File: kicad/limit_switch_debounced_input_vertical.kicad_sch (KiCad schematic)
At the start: 4 parts, among them J1601 TBH-1x02-3.5mm, U1601 MAX6816

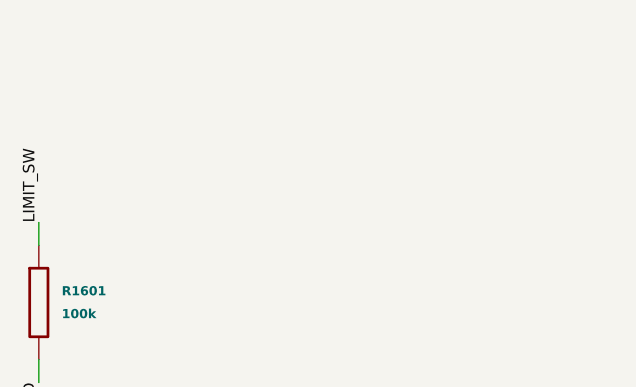
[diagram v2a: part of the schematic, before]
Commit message: Update limit switch block
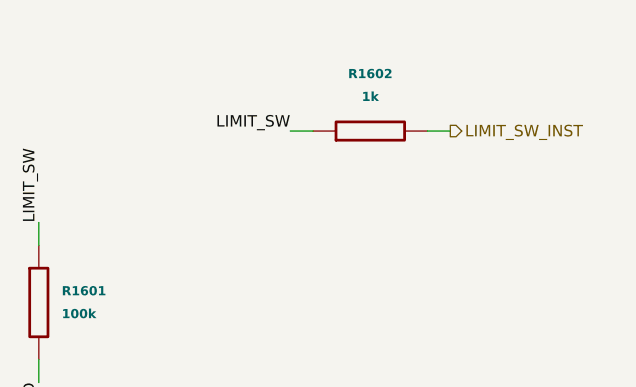
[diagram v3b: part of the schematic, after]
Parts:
- added R1602: 1k, Resistor_SMD:R_0402_1005Metric, symbol orb_weaver_internal:All/OW-PASS-RC0402FR-071KL
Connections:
- net LIMIT_SW: now also R1602.1
- new net LIMIT_SW_INST: R1602.2
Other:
- company: Janelia Research Campus -> (none)
- title: mouse-joystick-pcb -> Orb Weaver Design Block Mining

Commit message: Regenerate schematics
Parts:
- C1601: JLC Qty 9978 -> (none); LCSC C162178 -> (none); Placement (none) -> beside ${ed1d27a5-4fdc-4e73-a297-77a8487eb0d8:REFERENCE}.4 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; Vendor SKU C162178 -> (none)
- J1601: JLC Qty 148 -> (none); LCSC C3019639 -> (none); Vendor SKU C3019639 -> (none)
- R1601: JLC Qty 9963 -> (none); LCSC C106234 -> (none); Placement (none) -> beside ${ed1d27a5-4fdc-4e73-a297-77a8487eb0d8:REFERENCE}.3 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; Vendor SKU C106234 -> (none)
- R1602: JLC Qty 10129 -> (none); LCSC C106235 -> (none); Vendor SKU C106235 -> (none)
- U1601: value MAX6816 -> MAX6816EUS+T; JLC Qty 98 -> (none); LCSC C41637 -> (none); Name MAX6816 -> MAX6816 switch debouncer; ReqValue MAX6816 -> MAX6816EUS+T; Vendor SKU C41637 -> (none)
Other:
- note added: "${1a5dbbac-981b-4337-8c39-817e15b42b3f:REFERENCE} (100 k) holds LIMIT_SW low while the debouncer is unpowered; ${fb894a4c-a934-4f36-81fc-dbadc5d06e8e:REFERENCE} (1 k) is the series tap from LIMIT_SW to LIMIT_SW_INST."
- note added: "${1a5dbbac-981b-4337-8c39-817e15b42b3f:REFERENCE}, 100 kohm from LIMIT_SW to GND (OW-PASS-RC0402JR-07100KL, LCSC C106234), is what defines it while that domain is down, and it is"
- note added: "${1a5dbbac-981b-4337-8c39-817e15b42b3f:REFERENCE}: Output pull-down for the unpowered state"
- note added: "${877edc0d-8517-4bfb-9a8a-87ef2f65742a:REFERENCE}: Vcc bypass for ${ed1d27a5-4fdc-4e73-a297-77a8487eb0d8:REFERENCE}"
- note added: "${fb560492-07c1-40ba-abbe-6bac76e602ff:REFERENCE} brings the dry contact onto IN (pin 2) and GND (pin 1); ${ed1d27a5-4fdc-4e73-a297-77a8487eb0d8:REFERENCE} debounces IN and drives LIMIT_SW from its push-pull OUT. ${877edc0d-8517-4bfb-9a8a-87ef2f65742a:REFERENCE} (100 nF) bypasses Vcc (pin 4) to GND (pin 1)."
- note added: "+3.3V_SW is off."
- note added: "0.200 mm netclass rule. Move a run before widening it and re-run DRC after any change here."
- note added: "0.4 mm on these centres is a 0.100 mm gap, which sits exactly on the JLCPCB routine copper floor in .kicad_dru and errors under any 0.2 mm"
- note added: "1. Switch terminal and debouncer"
- note added: "100 kohm AND NOT 10 kohm: this net idles HIGH, since a normally-open contact plus the internal IN pull-up puts OUT high whenever the axis is away"
- note added: "2. Output pull-down and instrument tap"
- note added: "Bring REFL to a labelled test pad at board level so a jumper can force a closure during bring-up. Add no capacitor on IN — it fights the debounce"
- note added: "Connect a dry-contact mechanical switch across the terminal; pin 1 is GND, pin 2 is the switch node, and the contact is polarity-agnostic. OUT"
- note added: "DESIGN CONTRACT"
- note added: "Debounced limit-switch input with its own 2-position 3.5 mm VERTICAL, top-entry pluggable screw terminal — Phoenix MCV 1,5/2-G-3,5,"
- note added: "Debounced limit-switch input with its own 2-position 3.5 mm VERTICAL, top-entry pluggable screw terminal — Phoenix MCV 1,5/2-G-3,5, OW-CONN-TBH-1X02-3P5-VERT, on the local orb_weaver_tht copy of the MCV footprint — plus a MAX6816 single switch debouncer and local Vcc decoupling."
- note added: "Debounced limit-switch input, vertical terminal | MAX6816, output pull-down, instrument tap"
- note added: "Debounced switch state, active low on contact closure and about 50 ms late; push-pull at Vcc levels while powered, held low by ${1a5dbbac-981b-4337-8c39-817e15b42b3f:REFERENCE} when"
- note added: "Debouncer supply, 2.7 to 5.5 V; bind it to the switched domain of whatever LIMIT_SW drives, so the debouncer cannot back-power a powered-down"
- note added: "Electrically identical to the horizontal limit_switch_debounced_input block, port for port and part for part including the pull-down: +3.3V_SW, GND,"
- note added: "GND, pin 2 IN"
- note added: "GND. A closed contact pulls IN low; OUT follows IN non-inverting after the debounce (20 to 80 ms, 50 ms typical), so LIMIT_SW is active low and"
- note added: "IN is complete inside ${ed1d27a5-4fdc-4e73-a297-77a8487eb0d8:REFERENCE}: internal pull-up 63 k typical, -25 to +25 V range, +/-15 kV air-gap ESD. No external pull-up, series resistor or"
- note added: "INTERFACES"
- note added: "IS THEREFORE 0.3 mm, not the 0.4 mm it was authored at, which puts the LIMIT_SW-to-GND gap at exactly 0.200 mm against a 0.200 mm netclass"
- note added: "Instrument tap of LIMIT_SW through ${fb894a4c-a934-4f36-81fc-dbadc5d06e8e:REFERENCE} (1 k), INSTRUMENT class; reads asserted while the switched rail is off."
- note added: "Instrument tap series resistor"
- note added: "KNOW THE POLARITY CONSEQUENCE BEFORE TRUSTING A CAPTURE: LIMIT_SW is active low, so this resistor makes an instrument tap read ASSERTED, limit"
- note added: "LIMIT_SW."
- note added: "Matching net labels are connected. Group order explains function; PCB placement priorities are stated below."
- note added: "OPERATION"
- note added: "OW-CONN-TBH-1X02-3P5-VERT, on the local orb_weaver_tht copy of the MCV footprint — plus a MAX6816 single switch debouncer and local Vcc"
- note added: "PLACE: ${1a5dbbac-981b-4337-8c39-817e15b42b3f:REFERENCE} sits above ${ed1d27a5-4fdc-4e73-a297-77a8487eb0d8:REFERENCE} with its LIMIT_SW pad on the OUT side, so LIMIT_SW and GND never need to cross; ${fb894a4c-a934-4f36-81fc-dbadc5d06e8e:REFERENCE} goes where LIMIT_SW leaves toward the"
- note added: "PLACE: Keep ${ed1d27a5-4fdc-4e73-a297-77a8487eb0d8:REFERENCE} next to ${fb560492-07c1-40ba-abbe-6bac76e602ff:REFERENCE} so IN stays short; nothing else connects to IN. Leave the 4.75 mm inboard keepout of the vertical terminal free, and give the enclosure an aperture"
- note added: "PLACE: Place ${877edc0d-8517-4bfb-9a8a-87ef2f65742a:REFERENCE} hard against pin 4 with a short return to pin 1."
- note added: "Project-local pending bench verification; promotable once a second board uses it."
- note added: "REQUIRED, not optional: THE MAX6816 HAS NO Ioff. With Vcc at 0 V its push-pull OUT is undefined, and a board that taps LIMIT_SW for instrumentation"
- note added: "ROUTE: +3.3V_SW has no reference-project class here (Default); the placing board classes the switched rail."
- note added: "ROUTE: LIMIT_SW and LIMIT_SW_INST leave through vias (port copper); LIMIT_SW_INST carries the INSTRUMENT class."
- note added: "ROUTE: The LIMIT_SW and GND runs share the corridor bounded by the IN pad on 0.5 mm centres: every track in the block is 0.3 mm, which leaves the LIMIT_SW-to-GND gap at exactly the"
- note added: "ROUTING THE PULL-DOWN IS TIGHT, AND IT IS AT THE LIMIT: ${1a5dbbac-981b-4337-8c39-817e15b42b3f:REFERENCE} sits above the MAX6816 with its LIMIT_SW pad on the same side as the IC's OUT"
- note added: "Return; terminal pin 1 (the switch's other side), the Vcc bypass and the output pull-down."
- note added: "Same circuit as limit_switch_debounced_input plus the tap. ${fb560492-07c1-40ba-abbe-6bac76e602ff:REFERENCE} (Phoenix MCV 1,5/2-G-3,5) is pad-identical to the horizontal MC 1,5 but"
- note added: "Signal path: ${fb560492-07c1-40ba-abbe-6bac76e602ff:REFERENCE} pin 2 -> IN -> ${ed1d27a5-4fdc-4e73-a297-77a8487eb0d8:REFERENCE} IN (pin 2) -> OUT (pin 3) -> LIMIT_SW, tapped through ${fb894a4c-a934-4f36-81fc-dbadc5d06e8e:REFERENCE} to LIMIT_SW_INST; ${fb560492-07c1-40ba-abbe-6bac76e602ff:REFERENCE} pin 1 is"
- note added: "Supply +3.3V from the SWITCHED power domain on any board where LIMIT_SW drives a chip that can be powered down: if the debouncer stays alive"
- note added: "Supply 2.7 to 5.5 V at 6 uA typical (UVLO 1.9 to 2.6 V). ${1a5dbbac-981b-4337-8c39-817e15b42b3f:REFERENCE} (100 k) defines LIMIT_SW low while +3.3V_SW is off, since the MAX6816 has no Ioff;"
- note added: "Switch debouncer"
- note added: "THIS BLOCK IS A FORK BY CHOICE, NOT BY GEOMETRY. Unlike usb2_vertical and pycontrol_behavior_port_rj45_boundary_vertical, whose land patterns are"
- note added: "Vertical switch terminal, pin 1"
- note added: "What actually changes is the mechanical envelope, and it inverts. Relative to pad 1 the horizontal courtyard runs x -2.45 to +5.95, y -2.00 to +8.25;"
- note added: "above it for the plug, the screw head and the wire loop."
- note added: "anchored on pin 1, with a 4.75 mm inboard courtyard and the wire leaving perpendicular to the board. Never rotate it 180 degrees to face outboard:"
- note added: "and degrades the ESD rating. Keep the decoupling hard against Vcc."
- note added: "and the board outline notes change — but the INBOARD KEEPOUT GROWS from 2.00 mm to 4.75 mm, so a swap in place can collide with whatever sits"
- note added: "and the wire loop."
- note added: "and then MOVING THE FOOTPRINT BY (-1.75, 0) so pad 1 returns to its old absolute position; skip that and the whole connector translates by 1.75"
- note added: "approach velocity so that delay cannot overshoot the mechanical stop."
- note added: "asserts late: bound the homing approach velocity."
- note added: "behind the connector even though no pad moved. DO NOT ROTATE 180 DEGREES to make the wire entry face outboard: pin order runs the same"
- note added: "capacitor on IN; a capacitor fights the debounce and degrades the ESD rating."
- note added: "conn-tbh-1x02-3p5, which docs/connector-orientation-plan.md specifies but which is not yet populated on any row — treat it as owed. Because the"
- note added: "consumer through OUT."
- note added: "decoupling. Four parts: nothing external belongs on the IN side, because the MAX6816 supplies its own IN pull-up and +/-15 kV ESD protection and"
- note added: "direction in both footprints, and rotating reverses it in board space, silently swapping GND and the switch node. The wire now leaves perpendicular to"
- note added: "drill at 3.50 mm pitch, pin order ascending in +x. The copper is a drop-in; only the footprint ANCHOR moves, because the horizontal is centred on"
- note added: "follows IN non-inverting after roughly 50 ms of debounce, so LIMIT_SW is ACTIVE LOW on switch closure and asserts ~50 ms late — bound homing"
- note added: "from the limit, so the pull-down conducts continuously in the normal state — 33 uA at 100 kohm against 330 uA at 10 kohm — and 100 kohm"
- note added: "here, because design_block_tools.py check counts only unconnected items and is blind to a clearance error."
- note added: "instances of one block gets its pull halved, and LIMIT_SW is point-to-point inside a single instance — place this block twice and you get two"
- note added: "instrument port."
- note added: "mm and drags every attached track with it. The two parts are genuinely interchangeable at the catalog level and belong to equiv_group"
- note added: "must put the tap buffer on the ALWAYS-ON rail — a buffer on the switched rail cannot observe the domain it is powering down with — so without this"
- note added: "needs no external pull-up, series resistor, or input capacitor — the fourth part is a 100 kohm pull-down on the OUTPUT, doing an unrelated job."
- note added: "netclass. There is room to move: the LIMIT_SW column can go about 0.5 mm further from GND, straight up out of OUT. Re-run DRC after any change"
- note added: "off."
- note added: "on rail state. A pull-up is not an alternative — it would have to reference the switched rail, which is at 0 V exactly when it would be needed."
- note added: "pads are identical, the two layouts stay transferable in either direction once the connector is shifted by (-1.75, 0)."
- note added: "path. IT BELONGS IN THE BLOCK, NOT AT BOARD LEVEL, and that does not contradict the usual rule: that rule exists because a net shared between two"
- note added: "pin, so the two nets never need to cross — but they share a corridor bounded by the IN pad and sit on 0.5 mm centres. EVERY TRACK IN THIS BLOCK"
- note added: "quadrature_encoder_input_5v_sn74lvc2g17, whose R30005/R30006 cover Ioff high-Z on that block's outputs for exactly this reason; the case here is"
- note added: "reached, whenever the switched rail is off. Defined-but-untrue is the deliberate trade against floating, and the analysis layer must gate the channel"
- note added: "resistor a live, non-Schmitt CMOS input sees a floating source every time the switched domain is cycled, which on that board is the normal reset"
- note added: "revision, decided 2026-08-16, so nothing downstream defines this net either."
- note added: "rule and the GND-to-IN-pad gap at 0.225 mm: DRC-clean with ZERO MARGIN on the first of those. Do not widen either run without moving it first —"
- note added: "spends no meaningful VOH margin either."
- note added: "stronger, because the SN74LVC2G17 has Ioff and the MAX6816 does not."
- note added: "switches, two debouncers and two independent LIMIT_SW nets, each with its own pull-down. The same call is already made in"
- note added: "that means +3V3_SW, and LIMIT_SW fans out to the TMC5130A REFL pin and to an always-on instrumentation buffer — it reaches no MCU GPIO in any"
- note added: "that swaps GND and the switch node in board space."
- note added: "the board, so the enclosure in ../mouse-joysticks-mech needs an aperture above the terminal plus clearance for the screw head, the mating plug,"
- note added: "the net idles high with a normally-open contact (about 33 uA at 3.3 V), so a capture on LIMIT_SW_INST reads asserted whenever the switched rail is"
- note added: "the pad array with pin 1 at (-1.75, 0) while the vertical puts pin 1 at the origin. Migrating an existing placement therefore means changing the part"
- note added: "the vertical runs x -2.95 to +6.45, y -4.75 to +3.50. The outboard overhang collapses from 8.25 mm to 3.50 mm, so the terminal can move inboard"
- note added: "unrelated to their horizontal counterparts, this footprint is pad-identical to the horizontal MC 1,5/2-G-3,5: both are 1.8 x 3.6 mm pads on a 1.2 mm"
- note added: "while its consumer does not, OUT back-powers that chip through its input pin, by a route a GPIO bus switch cannot cover. On mouse-joystick-pcb"
- company: (none) -> Orb Weaver
- title: Orb Weaver Design Block Mining -> Debounced limit-switch input, vertical terminal
- moved on the sheet: C1601, J1601, R1601, R1602, U1601
